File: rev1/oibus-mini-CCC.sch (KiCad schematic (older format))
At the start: 52 parts, among them IC1 LDO40LPU33RY, J1 172310-1202, J3 S5B-ZR-SM4A-TF, J5 uavcan, P1 TC2030-MCP, SW1 SW_Push, U1 NINA-B311-00B, U2 SAM-M8Q, U3 SHT31-DIS-B, U5 DS28E05, U6 TCAN330, U7 STM32F303CCTx, Y1 16M

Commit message: defined power budget and DC-DC converters components; added to schematics incl. footprints
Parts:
- removed C2: 1u, Capacitor_SMD:C_0603_1608Metric, symbol Device:C
- removed C3: 4.7u, Capacitor_SMD:C_0805_2012Metric, symbol Device:C
- removed IC1: LDO40LPU33RY, LDO40LPURY:SON95P300X300X90-7N-D, symbol LDO40LPURY:LDO40LPURY
- removed J1: 172310-1202, lib_fp_global:MOLEX_172310-1202, symbol 172310-1202:172310-1202
- removed J5: uavcan, lib_fp_global:uavcan_connector, symbol uavcan_connector:uavcan
- removed JP1: Jumper_3_Bridged12, Jumper:SolderJumper-3_P1.3mm_Open_RoundedPad1.0x1.5mm, symbol Jumper:SolderJumper_3_Open
- removed U5: DS28E05, Package_TO_SOT_SMD:SOT-23, symbol OIBUS_20:DS28E05
- added BT1: Battery_Cell, Connector_JST:JST_PH_S2B-PH-K_1x02_P2.00mm_Horizontal, symbol Device:Battery_Cell
- added C1, C3: 1u, Capacitor_SMD:C_0603_1608Metric, symbol Device:C_Small
- added C12: 10n, Capacitor_SMD:C_0603_1608Metric, symbol Device:C_Small
- added C13, C9: 10u, Capacitor_SMD:C_0805_2012Metric, symbol Device:C
- added C4, C7, C8: 4u7, Capacitor_SMD:C_0805_2012Metric, symbol Device:C
- added D1: MBR120, Diode_SMD:D_0603_1608Metric, symbol Device:D_Schottky
- added J2: USB_B_Micro, Connector_USB:USB_Micro-B_Molex-105017-0001, symbol Connector:USB_B_Micro
- added J3: uavcan_5pins, lib_fp_global:Molex_PicoBlade_53048-0510_1x05_P1.25mm_Horizontal, symbol uavcan_connector:uavcan_5pins
- added L1: 4u7, Inductor_SMD:L_Wuerth_MAPI-3010, symbol Device:L
- added Q1: DMG3415U-7, Package_TO_SOT_SMD:SOT-23, symbol Device:Q_PMOS_GSD
- added R1, R6: 100k, Resistor_SMD:R_0603_1608Metric, symbol Device:R
- added R12: 4.7k, Resistor_SMD:R_0603_1608Metric, symbol Device:R
- added R2: 2k, Resistor_SMD:R_0603_1608Metric, symbol Device:R
- added R4, R7: 309k, Resistor_SMD:R_0603_1608Metric, symbol Device:R
- added U1: AP2112K-3.3, Package_TO_SOT_SMD:SOT-23-5, symbol Regulator_Linear:AP2112K-3.3
- added U4: MCP73831-2-OT, Package_TO_SOT_SMD:SOT-23-5, symbol Battery_Management:MCP73831-2-OT
- added U5: MCP1624T, Package_TO_SOT_SMD:SOT-23-6, symbol Regulator_Switching:MCP1640BCH
- R3: renamed from R7; value 330R -> 430R
- R5: value 4.7k -> 976k
- renumbered C19 to C10, C20 to C11, C11 to C14, C7 to C15, C8 to C16, C9 to C17, C10 to C18, C12 to C19, C1 to C2, C13 to C20, C14 to C21, C15 to C22, C16 to C23, C17 to C5, C18 to C6, D6 to D2, D5 to D3, D1 to D4, D2 to D5, D4 to D6, J3 to J1, JP2 to JP1, L1 to L2, R8 to R10, R9 to R11, R4 to R8, R6 to R9, U1 to U3, U3 to U6, U6 to U7, U7 to U8
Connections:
- net labels added: +BATT, 5V_EN, BAT_MEAS, USB_DM, USB_DP, VIN
- net labels removed: V_ANALOG_EN
- wire segments 233 -> 307
- no-connect marks 22 -> 20
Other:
- note added: "2kOhm —> max. \ncharging current of 500mA"
- note removed: "Vout = 1.2V * (1+4k7/1k5) = 4.96V"
- moved on the sheet: C14, C2, D3, R10, R11, R3

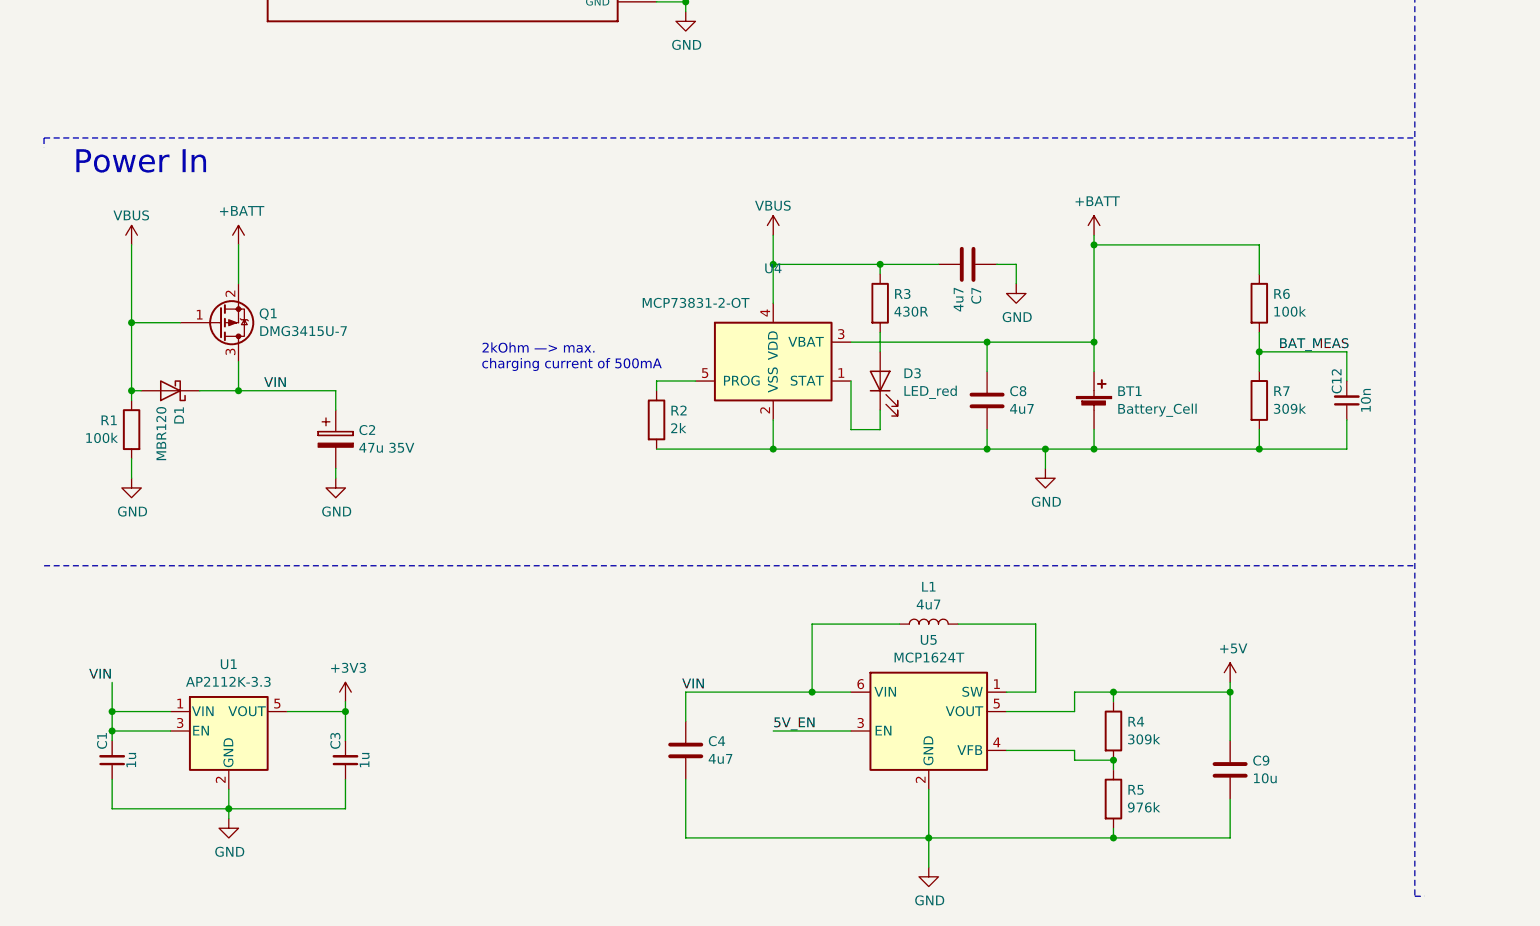
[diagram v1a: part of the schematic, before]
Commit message: added battery protection circuit to allow connecting unprotected Li-Ion cells
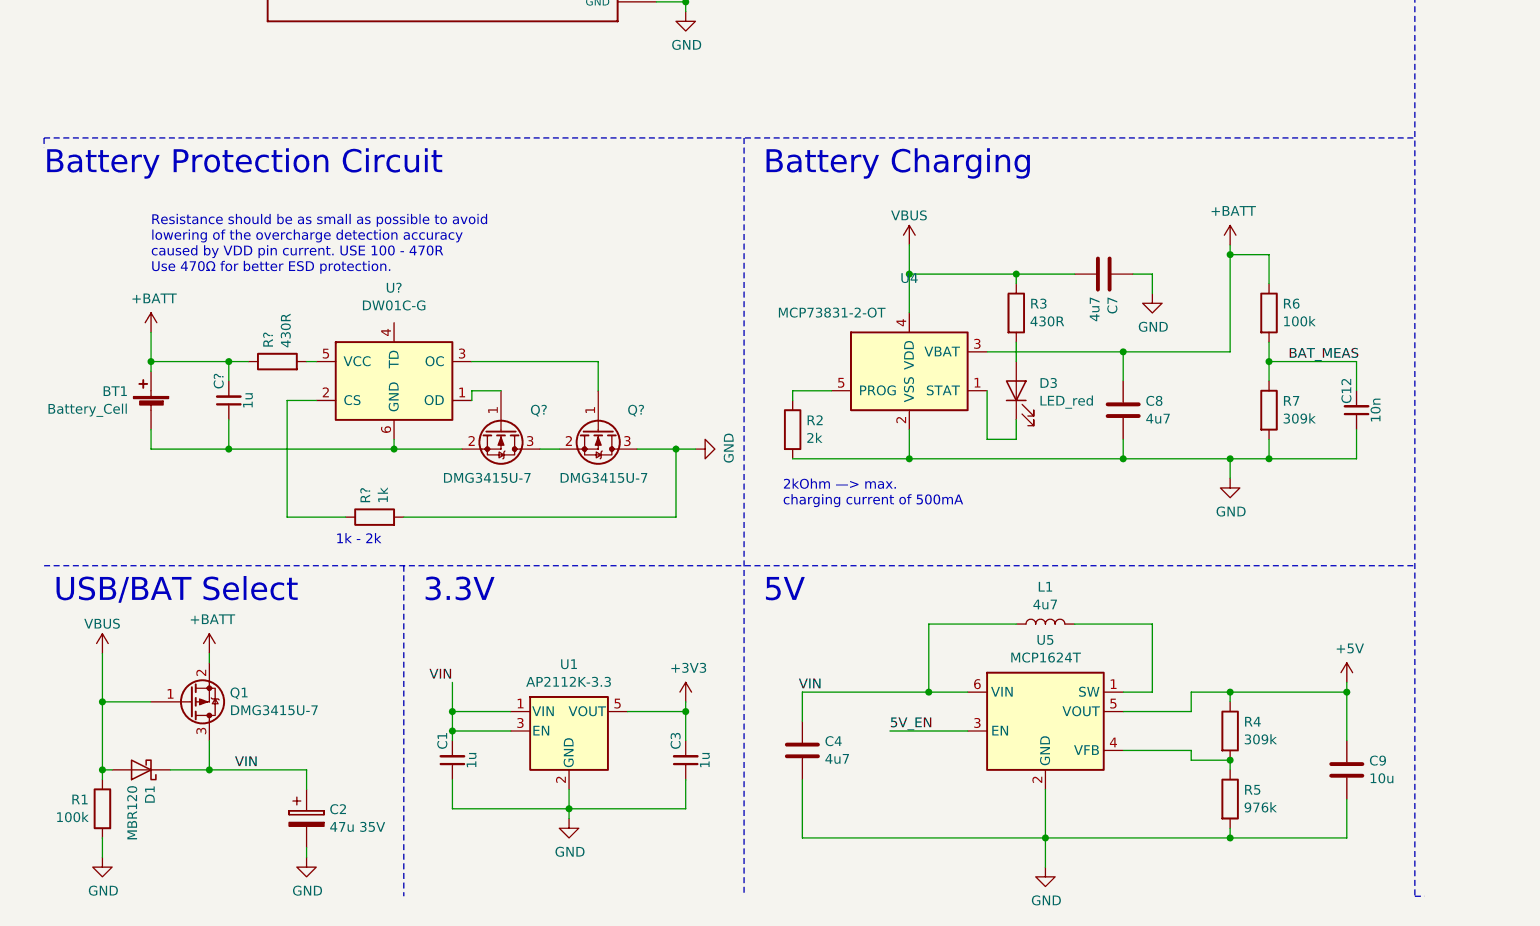
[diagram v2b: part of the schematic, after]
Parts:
- added C?: 1u, Capacitor_SMD:C_0603_1608Metric, symbol Device:C_Small
- added Q? (x2): DMG3415U-7, Package_TO_SOT_SMD:SOT-23, symbol Device:Q_NMOS_GSD
- added R?: 430R, Resistor_SMD:R_0603_1608Metric, symbol Device:R
- added R?: 1k, Resistor_SMD:R_0603_1608Metric, symbol Device:R
- added U?: DW01C-G, Package_SON:WSON-6_1.5x1.5mm_P0.5mm, symbol DW01:DW01
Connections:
- wire segments 307 -> 328
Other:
- note added: "1k - 2k"
- note added: "3.3V\n"
- note added: "5V\n"
- note added: "Battery Charging"
- note added: "Battery Protection Circuit"
- note added: "Resistance should be as small as possible to avoid \nlowering of the overcharge detection accuracy \ncaused by VDD pin current. USE 100 - 470R\nUse 470Ω for better ESD protection."
- note added: "USB/BAT Select"
- note removed: "Power In"
- moved on the sheet: BT1, C1, C12, C2, C3, C4, C7, C8, C9, D1, D3, L1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

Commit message: finished all pin assignments. pushed to layout
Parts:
- removed D2: D, Diode_SMD:D_0603_1608Metric, symbol Device:D
- removed JP1: SolderJumper_2_Open, Jumper:SolderJumper-2_P1.3mm_Open_RoundedPad1.0x1.5mm, symbol Jumper:SolderJumper_2_Open
- added C25, C26: 10p, Capacitor_SMD:C_0603_1608Metric, symbol Device:C_Small
- added D7: LED_ABRG, LED_SMD:LED_RGB_1210, symbol Device:LED_ABRG
- added J4: Conn_01x02_Female, Connector_PinHeader_2.00mm:PinHeader_1x02_P2.00mm_Vertical, symbol Connector:Conn_01x02_Female
- added R15, R16: 1k, Resistor_SMD:R_0603_1608Metric, symbol Device:R
- added R17: 2k7, Resistor_SMD:R_0603_1608Metric, symbol Device:R
- added Y2: 32kHz, Crystal:Crystal_SMD_SeikoEpson_FA238-4Pin_3.2x2.5mm, symbol Device:Crystal_GND24_Small
- gave numbers to parts that had none: 6
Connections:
- net labels added: BLUE, GREEN, NINA_CTS, NINA_DSR, NINA_DTR, NINA_RTS, RED
- net labels removed: EEPROM, P1, P2, P3, P4, TEMP_SENSOR
- wire segments 328 -> 361
- no-connect marks 20 -> 40
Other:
- note added: "The DSR pin can be used to:\n Enter the command mode\n Disconnect and/or toggle connectable status\n Enable/disable the rest of the UART interface\n Enter/wake up from the sleep mode"
- moved on the sheet: C14, C15, C16, C17, D4, D6, H2, J3, R10, R11, R12, R8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

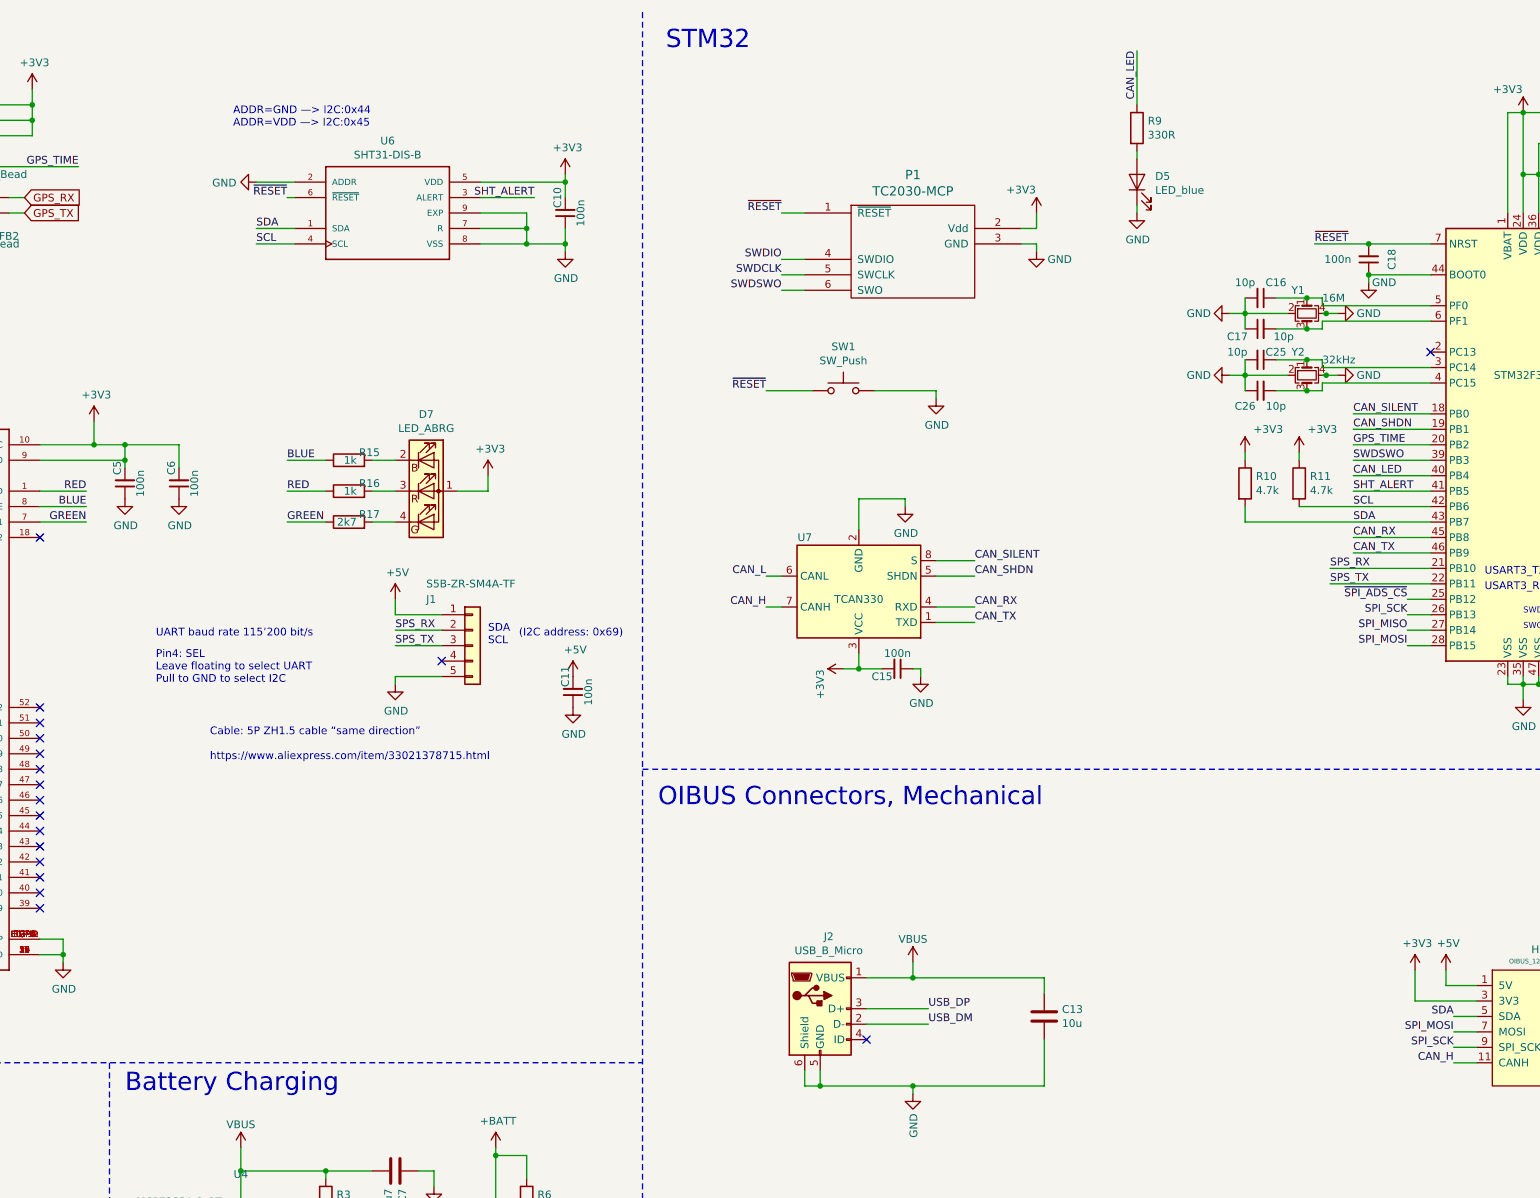
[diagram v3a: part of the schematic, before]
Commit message: grove connector and boot pin correction. added Licence file
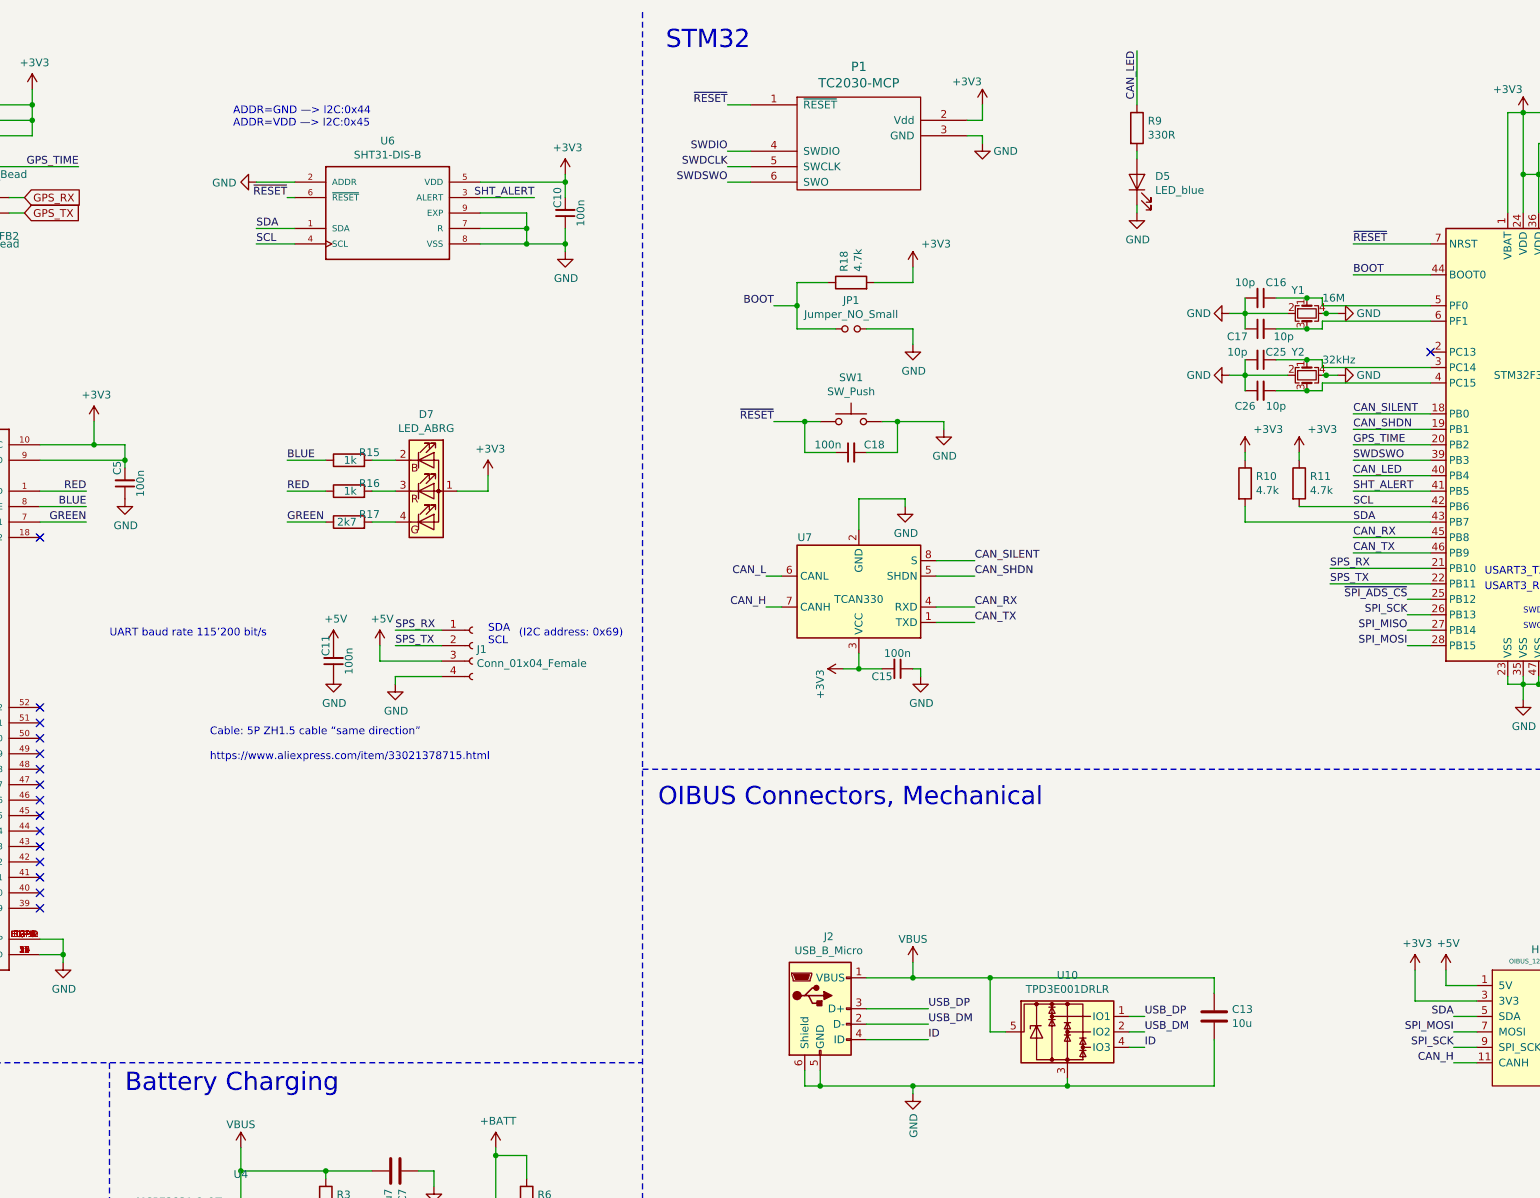
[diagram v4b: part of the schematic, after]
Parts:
- removed C6: 100n, Capacitor_SMD:C_0603_1608Metric, symbol Device:C_Small
- removed J1: S5B-ZR-SM4A-TF, lib_fp:JST_S5B-ZR-SM4A-TF, symbol Connector_Generic:Conn_01x05
- added J1: Conn_01x04_Female, lib_fp:Grove_1x04, symbol Connector:Conn_01x04_Female
- added JP1: Jumper_NO_Small, Jumper:SolderJumper-2_P1.3mm_Open_RoundedPad1.0x1.5mm, symbol Device:Jumper_NO_Small
- added R18: 4.7k, Resistor_SMD:R_0603_1608Metric, symbol Device:R
- added U10: TPD3E001DRLR, Package_TO_SOT_SMD:SOT-553, symbol Power_Protection:TPD3E001DRLR
- C23: MPN 885012206089 -> (none)
- J2: LCSC (none) -> C10418; MPN C10418 -> (none)
- Q1, Q2, Q3: MPN (none) -> DMG3415U-7
- U1: MPN (none) -> AP2112K-3.3
- U2: MPN (none) -> SAM-M8Q
- U3: MPN (none) -> NINA-B311-00B
- U4: MPN (none) -> MCP73831-2-OT
- U5: MPN (none) -> MCP1624T
- U6: MPN (none) -> SHT31-DIS-B
- U9: MPN (none) -> DW01C-G
- Y2: LCSC (none) -> C97604; MPN (none) -> SC32S-7PF20PPM
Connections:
- net +3V3: now also R18.2
- net +5V: now also J1.3 (Pin_3)
- net GND: now also C18.2, J1.4 (Pin_4), JP1.1, U10.3; no longer C18.1, U8.44 (BOOT0)
- net SPS_RX: now also J1.1 (Pin_1)
- net SPS_TX: now also J1.2 (Pin_2)
- net USB_DM: now also U10.2 (IO2)
- net USB_DP: now also U10.1 (IO1)
- net VBUS: now also U10.5
- net ~RESET: now also C18.1; no longer C18.2
- net ID: now reaches J2.4 (ID)
- net ID: now also U10.4 (IO3)
- new net BOOT: JP1.2, R18.1, U8.44 (BOOT0)
- no-connect marks 40 -> 38
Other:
- note removed: "Pin4: SEL\nLeave floating to select UART\nPull to GND to select I2C"
- moved on the sheet: C11, C13, C18, P1, SW1

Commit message: finished component placement
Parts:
- removed C13: 10u, Capacitor_SMD:C_0805_2012Metric, symbol Device:C
- J4: footprint Connector_PinHeader_2.00mm:PinHeader_1x02_P2.00mm_Vertical -> Jumper:SolderJumper-2_P1.3mm_Open_RoundedPad1.0x1.5mm
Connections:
- net USB_DM: now also U10.1 (IO1); no longer U10.2 (IO2)
- net USB_DP: now also U10.2 (IO2); no longer U10.1 (IO1)
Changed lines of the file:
@@
 Wire Wire Line
 	9300 6750 9000 6750
-$Comp
-L Device:C C13
-U 1 1 5E2F9E1B
-P 11250 7000
-F 0 "C13" H 11135 6954 50  0000 R CNN
-F 1 "10u" H 11135 7045 50  0000 R CNN
-F 2 "Capacitor_SMD:C_0805_2012Metric" H 11288 6850 50  0001 C CNN
-F 3 "~" H 11250 7000 50  0001 C CNN
-	1    11250 7000
-	-1   0    0    1
-$EndComp
-Wire Wire Line
-	11250 6750 11250 6850
 Connection ~ 9300 6750
-Wire Wire Line
-	11250 7150 11250 7450
 Wire Wire Line
 	8700 7450 8700 7350
@@
 F 0 "J4" H 844 4475 50  0000 C CNN
 F 1 "Conn_01x02_Female" H 844 4566 50  0000 C CNN
-F 2 "Connector_PinHeader_2.00mm:PinHeader_1x02_P2.00mm_Vertical" H 950 4800 50  0001 C CNN
+F 2 "Jumper:SolderJumper-2_P1.3mm_Open_RoundedPad1.0x1.5mm" H 950 4800 50  0001 C CNN
 F 3 "~" H 950 4800 50  0001 C CNN
 	1    950  4800
@@
 Wire Wire Line
 	9300 6750 9800 6750
-Connection ~ 9800 6750
-Wire Wire Line
-	9800 6750 11250 6750
+Text Label 10800 7100 0    50   ~ 0
+USB_DP
+Wire Wire Line
+	10800 7000 10700 7000
 Text Label 10800 7000 0    50   ~ 0
-USB_DP
-Wire Wire Line
-	10800 7000 10700 7000
-Text Label 10800 7100 0    50   ~ 0
 USB_DM
 Wire Wire Line
@@
 Wire Wire Line
 	10300 7450 10300 7400
-Connection ~ 10300 7450
-Wire Wire Line
-	10300 7450 11250 7450
 Wire Wire Line
 	9000 7150 9400 7150
